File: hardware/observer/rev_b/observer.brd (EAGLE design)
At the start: 47.8 x 59.9 mm, 48 parts, among them J1 CON_HEADER_2X05-SMD+SHROUDED, J2 CON_HEADER_2X05-SMD+SHROUDED, J3 TC2030-CC2538-BL-NL, J4 JUMPER-PTH-2-NO, J5 PINHD-2X8/SMD, J6 CON_HEADER_2X05-PTH+SHROUDED_A, P9/P8 BBB_HEADER, U1 LPS331AP, U2 MPU-9250, U3 SI1147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

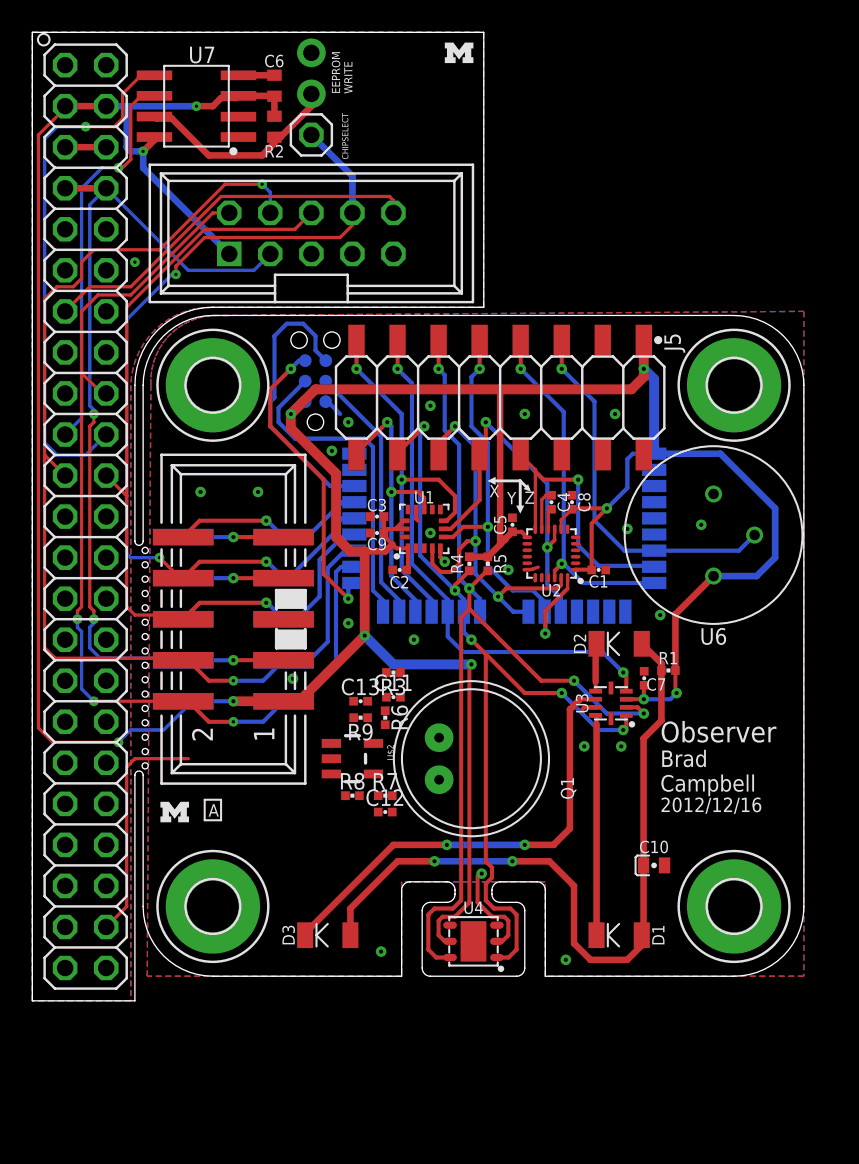
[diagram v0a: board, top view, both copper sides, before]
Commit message: Finished routing, needs to be looked over for correctness
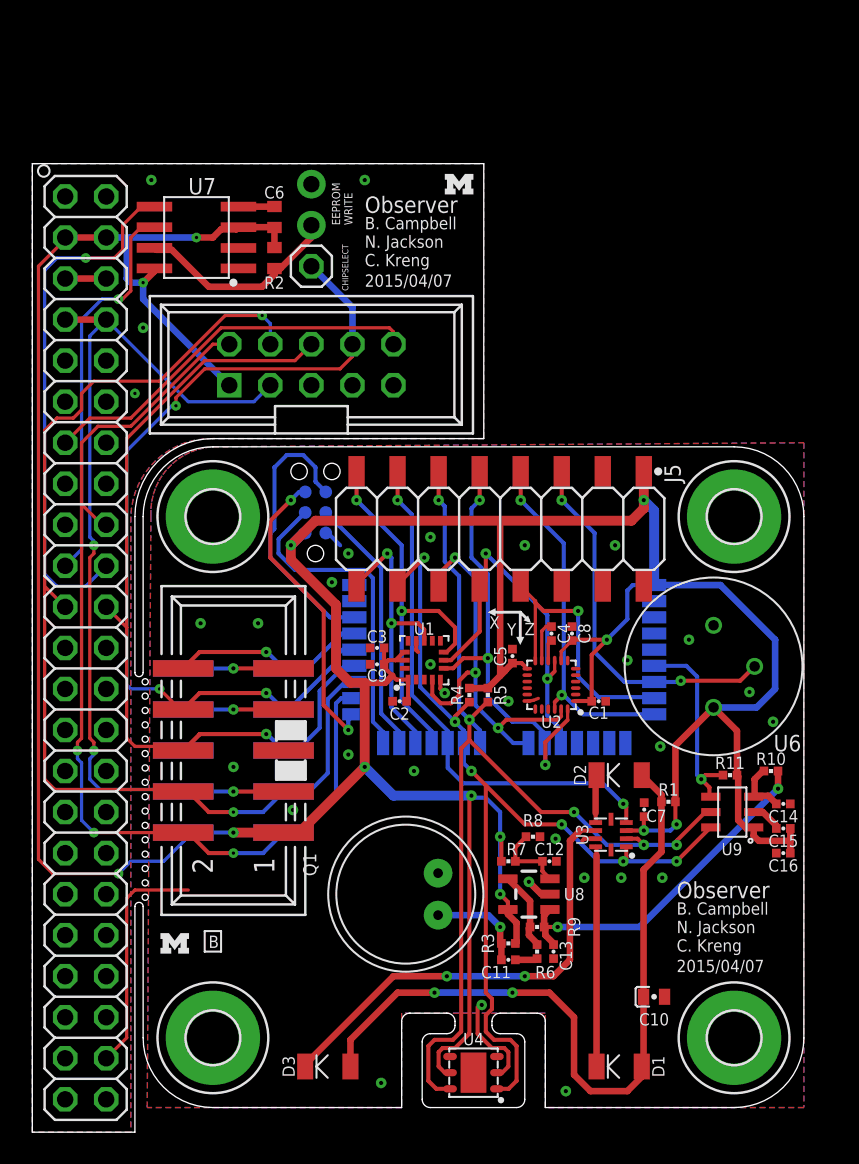
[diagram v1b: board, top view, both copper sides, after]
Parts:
- removed U$2: OPA344, SparkFun-AnalogIC:SOT23-5
- added C14: 470pF, passives:0402_CAP
- added C15: 4.7uF, passives:0402_CAP
- added C16: 0.1uF, passives:0402_CAP
- added R10: 22, passives:0402_RES
- added R11: 5k, passives:0402_RES
- added U8: OPA344, SparkFun-AnalogIC:SOT23-5
- added U9: ADC121C021, observer:ADC121C021
- moved C13 19.6 mm to (32.3, 11.2), turned to 270 degrees
- moved R3 18.2 mm to (29.5, 11.7), turned to 0 degrees
- moved C11 17.7 mm to (29.5, 10.7), turned to 180 degrees
- moved R6 17.3 mm to (31.2, 11.2), turned to 90 degrees
- moved R9 16.9 mm to (31.2, 12.7), turned to 0 degrees
- moved R8 11.5 mm to (31.0, 18.3), turned to 180 degrees
- moved C12 10.6 mm to (32.0, 16.8)
- moved Q1 9.32 mm to (23.1, 14.7), turned to 270 degrees
- moved R7 8.64 mm to (29.5, 16.8), turned to 180 degrees
- moved LOGO2 8.13 mm to (26.4, 58.7)
- moved C9 8.13 mm to (21.3, 29.0)
- moved R4 8.13 mm to (27.1, 27.1)
- moved R5 8.13 mm to (28.2, 27.1)
- moved C10 8.13 mm to (38.5, 8.38)
- moved LOGO1 8.13 mm to (8.81, 11.7)
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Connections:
- new net N$11: C14.1, R10.2, U9.VIN
- net GND: now also C14.2, C15.2, C16.2, U8.2, U9.GND; no longer U$2.2
- net MIC_AIN: now also R10.1, U8.1; no longer U$2.1
- net MIC_INT: now also R11.1, U9.ALRT
- net N$10: now also U8.3; no longer U$2.3
- net N$9: now also U8.4; no longer U$2.4
- net SCL: now also U9.SCL
- net SDA: now also U9.SDA
- net VCC: now also C15.1, C16.1, R11.2, U8.5, U9.VA; no longer U$2.5
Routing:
- net VCC: track 230.3 -> 255.9 mm, vias 11 -> 13
- net MIC_AIN: track 0.00 -> 21.8 mm, vias 0 -> 2
- net MIC_INT: track 0.00 -> 12.2 mm, vias 0 -> 1
- net SDA: track 52.8 -> 59.1 mm, vias 5 -> 6
- net N$1: track 0.00 -> 6.21 mm, vias 0 -> 1
- net SCL: track 59.9 -> 65.0 mm, vias 4 -> 5
- net N$9: track 0.00 -> 4.88 mm
- net N$10: track 0.00 -> 4.74 mm
- net GND: track 35.7 -> 39.3 mm, vias 22 -> 31
- net N$11: track 0.00 -> 3.45 mm
- net N$5: track 0.00 -> 1.38 mm
- net PIR_OUT: vias 1 -> 2
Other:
- board text added: "2015/04/07"
- board text added: "B"
- board text added: "B. Campbell N. Jackson C. Kreng"
- board text removed: "2012/12/16"
- board text removed: "A"
- board text removed: "Brad Campbell"

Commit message: Fixed header on motherboard, added decoupling cap for op amp
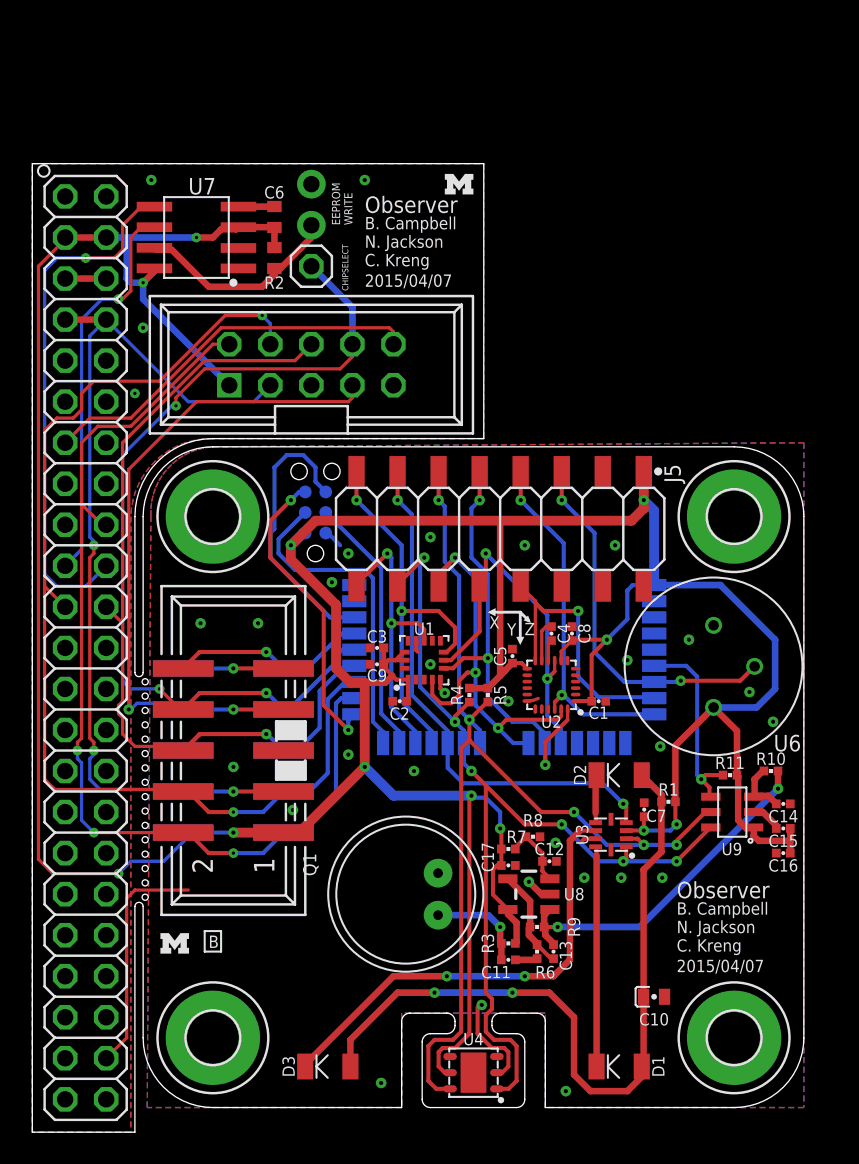
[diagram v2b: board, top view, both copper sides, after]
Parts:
- added C17: 0.1uF, passives:0402_CAP
- moved R7 0.76 mm to (29.5, 17.5)
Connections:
- net !OBSERVER_CS renamed !OBS_CS
- removed net N$119: J6.7
- net BBB_GPIO: now also J6.7
- net GND: now also C17.2
- net N$9: now also C13.2
- net VCC: now also C17.1
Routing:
- net BBB_GPIO: track 6.21 -> 41.2 mm, vias 1 -> 2
- net N$9: track 4.88 -> 6.26 mm
- net VCC: track 255.9 -> 254.9 mm, vias 13 -> 12

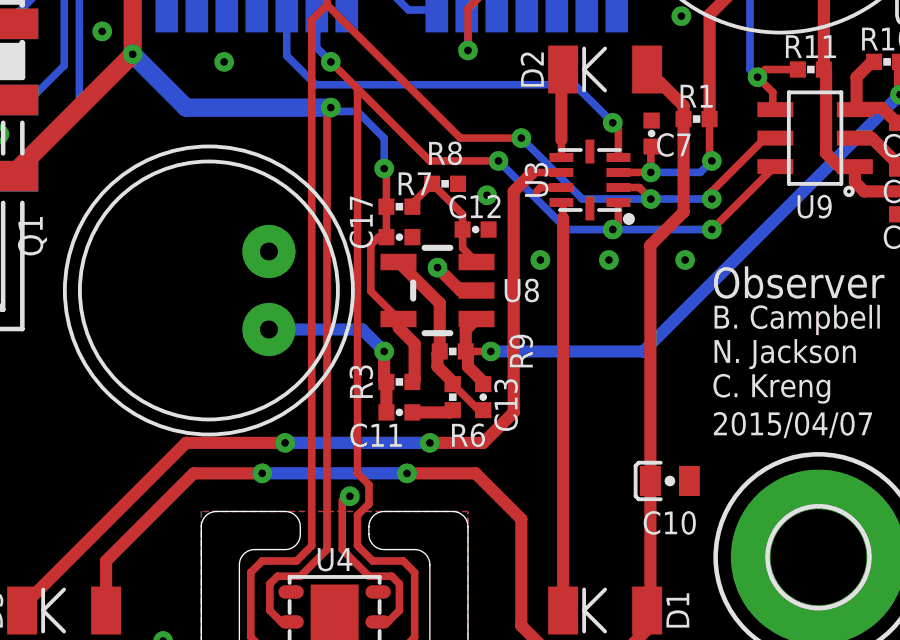
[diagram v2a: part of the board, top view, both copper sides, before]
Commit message: fixed some spacing issues
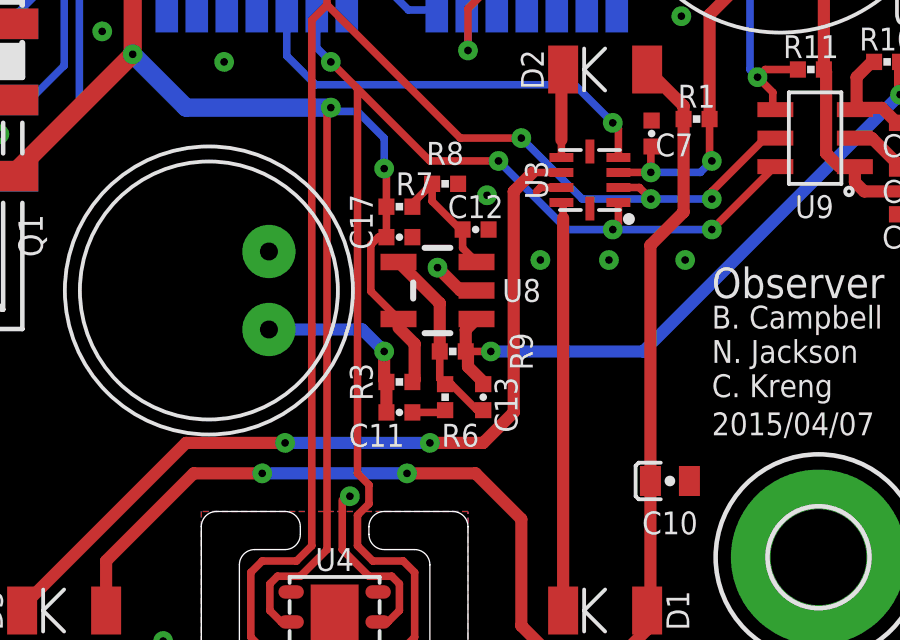
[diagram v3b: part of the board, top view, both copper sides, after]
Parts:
- moved R6 0.25 mm to (31.0, 11.2)
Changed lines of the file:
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@@
 </class>
 </classes>
-<designrules name="sunstone-2lyr_v1.0.0.3 *">
+<designrules name="sunstone-2lyr_v1.0.0.3">
 <description language="en">&lt;b&gt;EAGLE Design Rules for *2* Layer Designs (DS)&lt;/b&gt;
 &lt;p&gt;
@@
 <param name="mdViaViaSameLayer" value="8mil"/>
 <param name="mnLayersViaInSmd" value="2"/>
-<param name="mdCopperDimension" value="10mil"/>
+<param name="mdCopperDimension" value="20mil"/>
 <param name="mdDrill" value="16mil"/>
 <param name="mdSmdStop" value="0mil"/>
@@
 <param name="mlMinCreamFrame" value="0mil"/>
 <param name="mlMaxCreamFrame" value="0mil"/>
-<param name="mlViaStopLimit" value="20mil"/>
+<param name="mlViaStopLimit" value="0mil"/>
 <param name="srRoundness" value="0"/>
 <param name="srMinRoundness" value="0mil"/>
@@
 <attribute name="VALUE" x="29.464" y="12.065" size="1.016" layer="27" font="vector" ratio="12" rot="R180" align="bottom-center"/>
 </element>
-<element name="R6" library="passives" package="0402_RES" value="10k" x="31.242" y="11.176" smashed="yes" rot="R90">
-<attribute name="NAME" x="31.75" y="10.287" size="0.762" layer="25" font="vector" ratio="12" rot="R180" align="bottom-center"/>
-<attribute name="VALUE" x="32.639" y="11.176" size="1.016" layer="27" font="vector" ratio="12" rot="R90" align="bottom-center"/>
+<element name="R6" library="passives" package="0402_RES" value="10k" x="30.988" y="11.176" smashed="yes" rot="R90">
+<attribute name="NAME" x="31.496" y="10.287" size="0.762" layer="25" font="vector" ratio="12" rot="R180" align="bottom-center"/>
+<attribute name="VALUE" x="32.385" y="11.176" size="1.016" layer="27" font="vector" ratio="12" rot="R90" align="bottom-center"/>
 </element>
 <element name="R7" library="passives" package="0402_RES" value="10k" x="29.464" y="17.526" smashed="yes" rot="R180">
@@
 <contactref element="C11" pad="1"/>
 <contactref element="R6" pad="1"/>
-<wire x1="29.89706875" y1="10.668" x2="31.16706875" y2="10.668" width="0.4064" layer="1"/>
-<wire x1="31.16706875" y1="10.668" x2="31.242" y2="10.74293125" width="0.4064" layer="1"/>
+<wire x1="29.89706875" y1="10.668" x2="30.91306875" y2="10.668" width="0.254" layer="1"/>
+<wire x1="30.91306875" y1="10.668" x2="30.988" y2="10.74293125" width="0.254" layer="1"/>
 </signal>
 <signal name="N$9">
@@
 <contactref element="U8" pad="4"/>
 <contactref element="R9" pad="1"/>
-<wire x1="31.242" y1="11.60906875" x2="31.242" y2="11.684" width="0.4064" layer="1"/>
-<wire x1="31.242" y1="11.684" x2="30.734" y2="12.192" width="0.4064" layer="1"/>
-<wire x1="30.734" y1="12.192" x2="30.734" y2="12.62506875" width="0.4064" layer="1"/>
-<wire x1="30.734" y1="12.62506875" x2="30.80893125" y2="12.7" width="0.4064" layer="1"/>
 <wire x1="30.80893125" y1="12.7" x2="30.80893125" y2="14.30696875" width="0.4064" layer="1"/>
 <wire x1="30.80893125" y1="14.30696875" x2="29.4339" y2="15.682" width="0.4064" layer="1"/>
 <contactref element="C13" pad="2"/>
 <wire x1="32.258" y1="10.74293125" x2="32.1081375" y2="10.74293125" width="0.254" layer="1"/>
-<wire x1="32.1081375" y1="10.74293125" x2="31.242" y2="11.60906875" width="0.254" layer="1"/>
+<wire x1="30.80893125" y1="12.7" x2="30.80893125" y2="11.7881375" width="0.254" layer="1"/>
+<wire x1="30.80893125" y1="11.7881375" x2="30.988" y2="11.60906875" width="0.254" layer="1"/>
+<wire x1="30.988" y1="11.60906875" x2="31.18993125" y2="11.60906875" width="0.254" layer="1"/>
+<wire x1="32.258" y1="10.74293125" x2="32.05606875" y2="10.74293125" width="0.254" layer="1"/>
+<wire x1="32.05606875" y1="10.74293125" x2="31.18993125" y2="11.60906875" width="0.254" layer="1"/>
 </signal>
 <signal name="N$10">
@@
 <wire x1="29.89706875" y1="17.6301375" x2="30.55493125" y2="18.288" width="0.254" layer="1"/>
 <wire x1="31.57093125" y1="16.14516875" x2="31.57093125" y2="16.764" width="0.254" layer="1"/>
-<wire x1="31.57093125" y1="16.764" x2="31.57093125" y2="17.272" width="0.254" layer="1"/>
-<wire x1="31.57093125" y1="17.272" x2="30.55493125" y2="18.288" width="0.254" layer="1"/>
+<wire x1="30.55493125" y1="18.288" x2="30.55493125" y2="17.70506875" width="0.254" layer="1"/>
+<wire x1="31.57093125" y1="16.764" x2="31.496" y2="16.764" width="0.254" layer="1"/>
+<wire x1="31.496" y1="16.764" x2="30.55493125" y2="17.70506875" width="0.254" layer="1"/>
 </signal>
 <signal name="MIC_AIN">

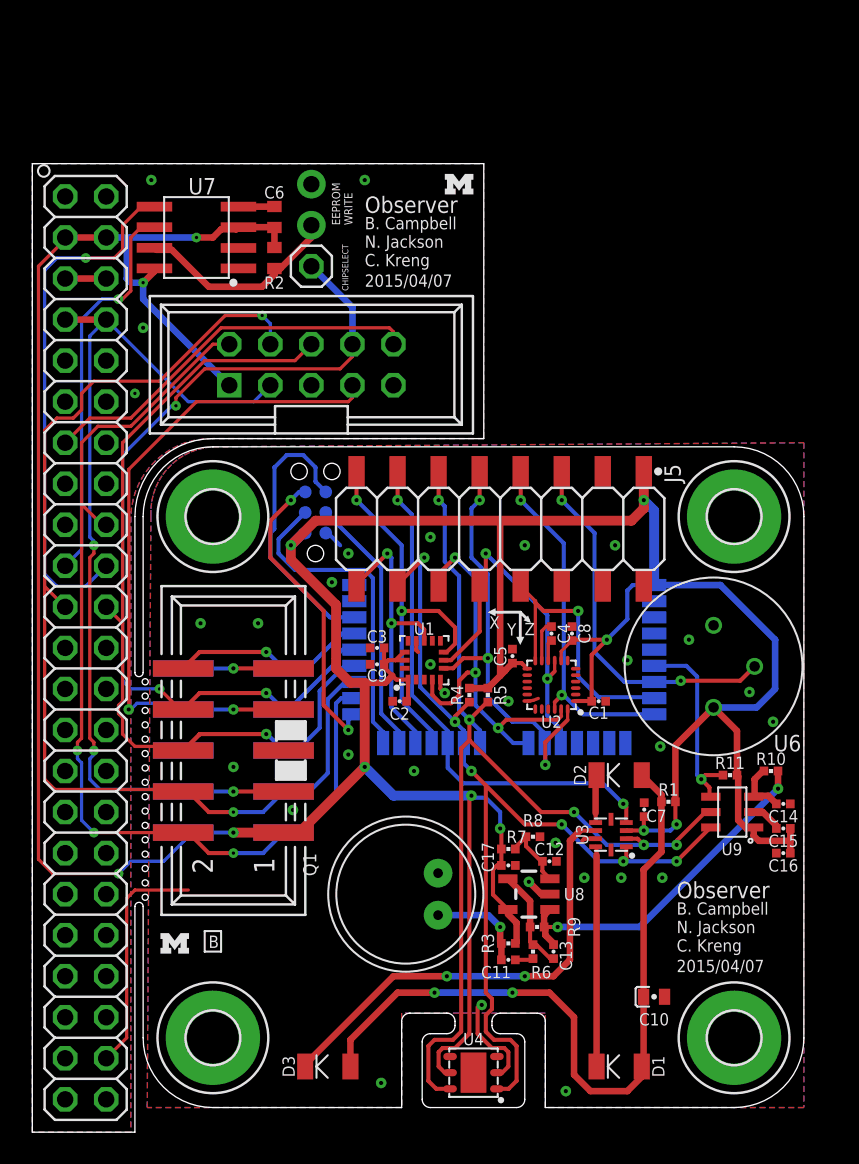
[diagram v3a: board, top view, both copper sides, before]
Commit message: Fixed clearance issues near BBB header and mousebites
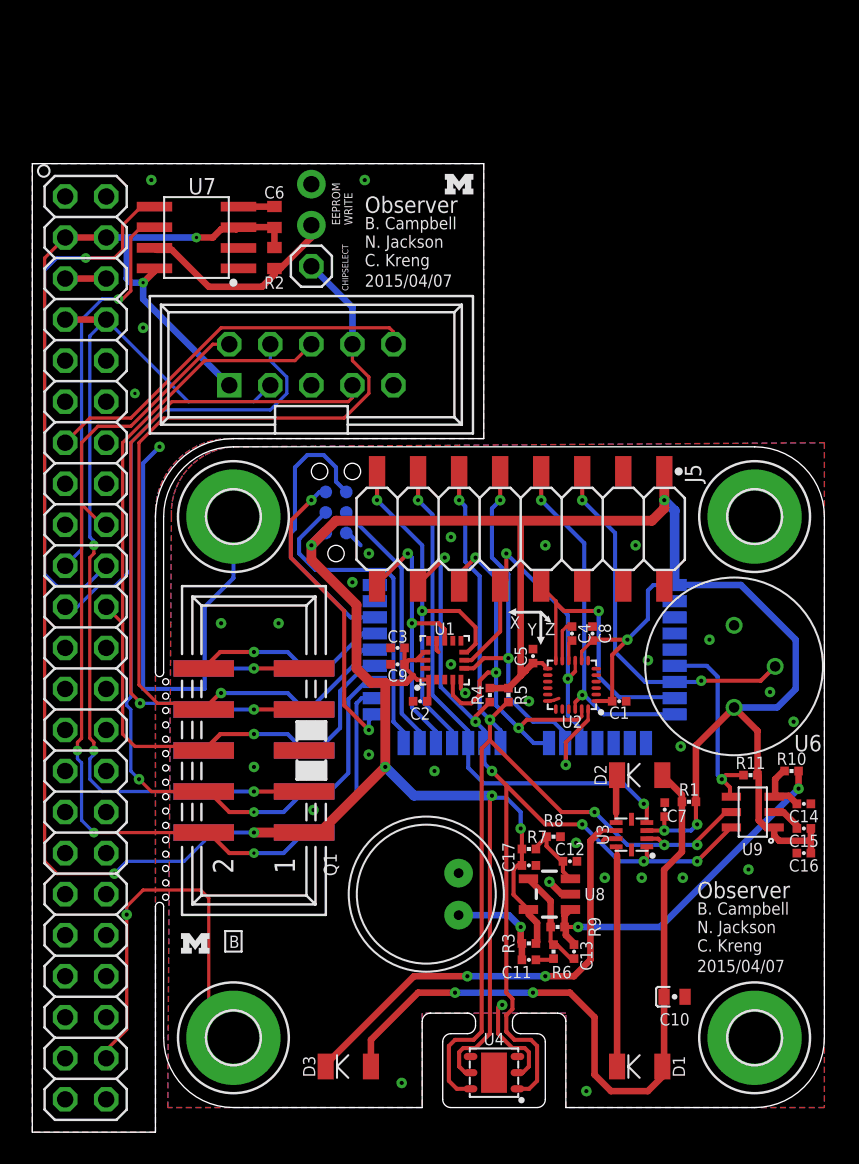
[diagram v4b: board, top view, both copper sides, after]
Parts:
- moved C1 1.27 mm to (36.3, 26.7)
- moved C11 1.27 mm to (30.7, 10.7)
- moved C12 1.27 mm to (33.3, 16.8)
- moved C14 1.27 mm to (47.8, 20.3)
- moved C15 1.27 mm to (47.8, 18.8)
- moved C16 1.27 mm to (47.8, 17.3)
- moved C17 1.27 mm to (30.7, 16.5)
- moved C3 1.27 mm to (22.6, 30.0)
- moved C4 1.27 mm to (33.4, 30.9)
- moved C9 1.27 mm to (22.6, 29.0)
- moved H5 1.27 mm to (44.7, 38.1)
- moved H6 1.27 mm to (44.7, 5.84)
- moved R1 1.27 mm to (40.6, 20.4)
- moved R10 1.27 mm to (47.0, 22.4)
- moved R11 1.27 mm to (44.5, 22.1)
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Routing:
- net GND: track 39.3 -> 80.3 mm, vias 31 -> 34
- net BBB_MISO: track 68.4 -> 62.1 mm
- net !OBS_CS: track 55.8 -> 57.8 mm, vias 3 -> 1
- net 5V: track 56.8 -> 58.2 mm
- net BBB_MOSI: track 62.3 -> 63.6 mm
- net BBB_GPIO: track 41.2 -> 42.4 mm
- net BBB_SCLK: track 54.5 -> 55.6 mm
- net VCC: track 254.9 -> 255.8 mm
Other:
- board size 47.8 x 59.9 mm -> 49 x 59.9 mm
